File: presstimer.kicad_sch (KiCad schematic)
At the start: 28 parts, among them J1 Screw_Terminal_01x02, SW1 SW_Push, SW2 SW_Push, U1 AP7361C-33ER, U2 ESP32-S3-WROOM-1

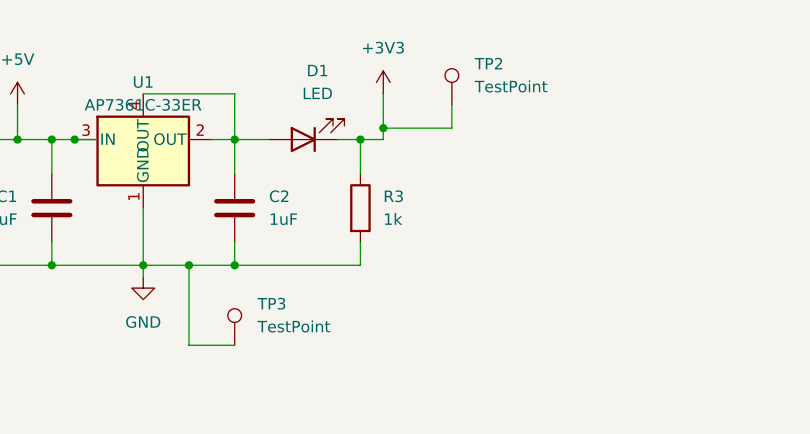
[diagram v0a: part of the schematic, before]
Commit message: fix: corrected 3v3 connections at D5, USB power to LDO, power to I2C expansion
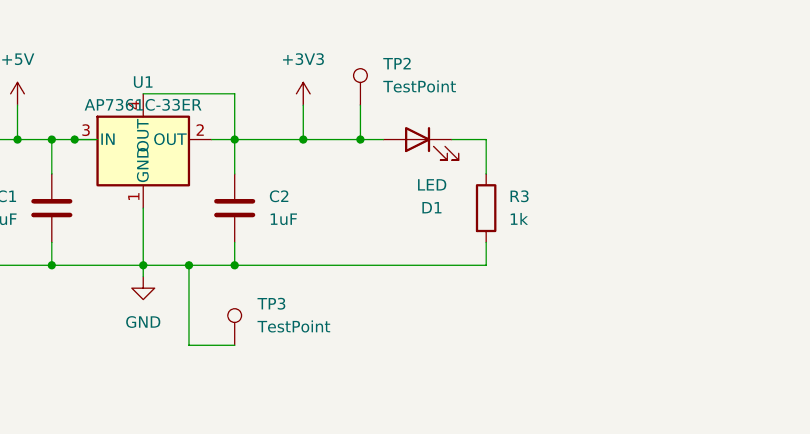
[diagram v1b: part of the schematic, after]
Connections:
- net +3V3: now also C2.1, D1.2 (A), U1.2 (OUT), U1.4 (OUT); no longer D1.1 (K), R3.1
- new net: D1.1 (K), R3.1
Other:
- moved on the sheet: D1, R3, TP2
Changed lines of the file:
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@@
 	)
 	(junction
-		(at 68.58 40.64)
+		(at 92.71 26.67)
 		(diameter 0)
 		(color 0 0 0 0)
 	)
 	(junction
-		(at 92.71 26.67)
+		(at 68.58 40.64)
 		(diameter 0)
 		(color 0 0 0 0)
 	)
 	(junction
-		(at 95.25 25.4)
+		(at 86.36 26.67)
 		(diameter 0)
 		(color 0 0 0 0)
@@
 	(wire
 		(pts
-			(xy 78.74 26.67) (xy 82.55 26.67)
+			(xy 78.74 26.67) (xy 86.36 26.67)
 		)
 		(stroke
@@
 	(wire
 		(pts
-			(xy 92.71 26.67) (xy 92.71 30.48)
+			(xy 106.68 26.67) (xy 106.68 30.48)
 		)
 		(stroke
@@
 	(wire
 		(pts
-			(xy 92.71 38.1) (xy 92.71 40.64)
+			(xy 106.68 38.1) (xy 106.68 40.64)
 		)
 		(stroke
@@
 	(wire
 		(pts
-			(xy 95.25 21.59) (xy 95.25 25.4)
+			(xy 92.71 22.86) (xy 92.71 26.67)
 		)
 		(stroke
@@
 	(wire
 		(pts
-			(xy 92.71 26.67) (xy 95.25 26.67)
-		)
-		(stroke
-			(width 0)
-			(type default)
-		)
-	)
-	(wire
-		(pts
 			(xy 182.88 60.96) (xy 182.88 59.69)
 		)
@@
 	(wire
 		(pts
-			(xy 95.25 25.4) (xy 95.25 26.67)
-		)
-		(stroke
-			(width 0)
-			(type default)
-		)
-	)
-	(wire
-		(pts
 			(xy 76.2 26.67) (xy 78.74 26.67)
 		)
@@
 	(wire
 		(pts
-			(xy 102.87 25.4) (xy 95.25 25.4)
-		)
-		(stroke
-			(width 0)
-			(type default)
-		)
-	)
-	(wire
-		(pts
 			(xy 248.92 135.89) (xy 248.92 138.43)
 		)
@@
 	(wire
 		(pts
-			(xy 102.87 22.86) (xy 102.87 25.4)
-		)
-		(stroke
-			(width 0)
-			(type default)
-		)
-	)
-	(wire
-		(pts
 			(xy 115.57 170.18) (xy 120.65 170.18)
 		)
@@
 	(wire
 		(pts
-			(xy 92.71 40.64) (xy 78.74 40.64)
+			(xy 106.68 40.64) (xy 78.74 40.64)
 		)
 		(stroke
@@
 	(wire
 		(pts
+			(xy 86.36 22.86) (xy 86.36 26.67)
+		)
+		(stroke
+			(width 0)
+			(type default)
+		)
+	)
+	(wire
+		(pts
 			(xy 72.39 146.05) (xy 78.74 146.05)
 		)
@@
 	(wire
 		(pts
-			(xy 58.42 146.05) (xy 64.77 146.05)
+			(xy 86.36 26.67) (xy 92.71 26.67)
 		)
 		(stroke
@@
 	(wire
 		(pts
-			(xy 31.75 29.21) (xy 38.1 29.21)
+			(xy 92.71 26.67) (xy 95.25 26.67)
+		)
+		(stroke
+			(width 0)
+			(type default)
+		)
+	)
+	(wire
+		(pts
+			(xy 58.42 146.05) (xy 64.77 146.05)
 		)
 		(stroke
@@
 	(wire
 		(pts
-			(xy 90.17 26.67) (xy 92.71 26.67)
+			(xy 31.75 29.21) (xy 38.1 29.21)
 		)
 		(stroke
@@
 	(wire
 		(pts
+			(xy 102.87 26.67) (xy 106.68 26.67)
+		)
+		(stroke
+			(width 0)
+			(type default)
+		)
+	)
+	(wire
+		(pts
 			(xy 58.42 26.67) (xy 60.96 26.67)
 		)
@@
 	(symbol
 		(lib_id "Connector:TestPoint")
-		(at 102.87 22.86 0)
+		(at 92.71 22.86 0)
 		(unit 1)
 		(body_style 1)
@@
 		(fields_autoplaced yes)
 		(property "Reference" "TP2"
-			(at 105.41 18.2879 0)
+			(at 95.25 18.2879 0)
 			(show_name no)
 			(do_not_autoplace no)
@@
 		)
 		(property "Value" "TestPoint"
-			(at 105.41 20.8279 0)
+			(at 95.25 20.8279 0)
 			(show_name no)
 			(do_not_autoplace no)
@@
 		)
 		(property "Footprint" "TestPoint:TestPoint_Pad_D1.5mm"
-			(at 107.95 22.86 0)
+			(at 97.79 22.86 0)
 			(hide yes)
 			(show_name no)
@@
 		)
 		(property "Datasheet" ""
-			(at 107.95 22.86 0)
+			(at 97.79 22.86 0)
 			(hide yes)
 			(show_name no)
@@
 		)
 		(property "Description" "test point"
-			(at 102.87 22.86 0)
+			(at 92.71 22.86 0)
 			(hide yes)
 			(show_name no)
@@
 	(symbol
 		(lib_id "power:+3V3")
-		(at 95.25 21.59 0)
+		(at 86.36 22.86 0)
 		(unit 1)
 		(body_style 1)
@@
 		(fields_autoplaced yes)
 		(property "Reference" "#PWR03"
-			(at 95.25 25.4 0)
+			(at 86.36 26.67 0)
 			(hide yes)
 			(show_name no)
@@
 		)
 		(property "Value" "+3V3"
-			(at 95.25 16.51 0)
+			(at 86.36 17.78 0)
 			(show_name no)
 			(do_not_autoplace no)
@@
 		)
 		(property "Footprint" ""
-			(at 95.25 21.59 0)
+			(at 86.36 22.86 0)
 			(hide yes)
 			(show_name no)
@@
 		)
 		(property "Datasheet" ""
-			(at 95.25 21.59 0)
+			(at 86.36 22.86 0)
 			(hide yes)
 			(show_name no)
@@
 		)
 		(property "Description" "Power symbol creates a global label with name \"+3V3\""
-			(at 95.25 21.59 0)
+			(at 86.36 22.86 0)
 			(hide yes)
 			(show_name no)
@@
 	(symbol
 		(lib_id "Device:R")
-		(at 92.71 34.29 0)
+		(at 106.68 34.29 0)
 		(unit 1)
 		(body_style 1)
@@
 		(fields_autoplaced yes)
 		(property "Reference" "R3"
-			(at 95.25 33.0199 0)
+			(at 109.22 33.0199 0)
 			(show_name no)
 			(do_not_autoplace no)
@@
 		)
 		(property "Value" "1k"
-			(at 95.25 35.5599 0)
+			(at 109.22 35.5599 0)
 			(show_name no)
 			(do_not_autoplace no)
@@
 		)
 		(property "Footprint" "PCM_JLCPCB:R_0603"
-			(at 90.932 34.29 90)
+			(at 104.902 34.29 90)
 			(hide yes)
 			(show_name no)
@@
 		)
 		(property "Datasheet" ""
-			(at 92.71 34.29 0)
+			(at 106.68 34.29 0)
 			(hide yes)
 			(show_name no)
@@
 		)
 		(property "Description" "Resistor"
-			(at 92.71 34.29 0)
+			(at 106.68 34.29 0)
 			(hide yes)
 			(show_name no)
@@
 		)
 		(property "LCSC" "C22548"
-			(at 95.25 33.0199 0)
+			(at 109.22 33.0199 0)
 			(hide yes)
 			(show_name no)
@@
 	(symbol
 		(lib_id "Device:LED")
-		(at 86.36 26.67 180)
+		(at 99.06 26.67 0)
+		(mirror y)
 		(unit 1)
 		(body_style 1)
@@
 		(in_pos_files yes)
 		(dnp no)
-		(fields_autoplaced yes)
 		(property "Reference" "D1"
-			(at 87.9475 19.05 0)
+			(at 100.6475 34.29 0)
 			(show_name no)
 			(do_not_autoplace no)
@@
 		)
 		(property "Value" "LED"
-			(at 87.9475 21.59 0)
+			(at 100.6475 31.75 0)
 			(show_name no)
 			(do_not_autoplace no)
@@
 		)
 		(property "Footprint" "PCM_JLCPCB:D_0805"
-			(at 86.36 26.67 0)
+			(at 99.06 26.67 0)
 			(hide yes)
 			(show_name no)
@@
 		)
 		(property "Datasheet" ""
-			(at 86.36 26.67 0)
+			(at 99.06 26.67 0)
 			(hide yes)
 			(show_name no)
@@
 		)
 		(property "Description" "Light emitting diode"
-			(at 86.36 26.67 0)
+			(at 99.06 26.67 0)
 			(hide yes)
 			(show_name no)
@@
 		)
 		(property "Sim.Pins" "1=K 2=A"
-			(at 86.36 26.67 0)
+			(at 99.06 26.67 0)
 			(hide yes)
 			(show_name no)
@@
 		)
 		(property "LCSC" "C84256"
-			(at 87.9475 19.05 0)
+			(at 100.6475 34.29 0)
 			(hide yes)
 			(show_name no)

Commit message: fixed ssr pinout
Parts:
- C3, C4, D1, D2, F1, R1, R13, R14, R2, R3: now in the parts list
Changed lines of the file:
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@@
 		(body_style 1)
 		(exclude_from_sim no)
-		(in_bom no)
+		(in_bom yes)
 		(on_board yes)
 		(in_pos_files yes)
@@
 		(body_style 1)
 		(exclude_from_sim no)
-		(in_bom no)
+		(in_bom yes)
 		(on_board yes)
 		(in_pos_files yes)
@@
 		(body_style 1)
 		(exclude_from_sim no)
-		(in_bom no)
+		(in_bom yes)
 		(on_board yes)
 		(in_pos_files yes)
@@
 		(body_style 1)
 		(exclude_from_sim no)
-		(in_bom no)
+		(in_bom yes)
 		(on_board yes)
 		(in_pos_files yes)
@@
 		(body_style 1)
 		(exclude_from_sim no)
-		(in_bom no)
+		(in_bom yes)
 		(on_board yes)
 		(in_pos_files yes)
@@
 		(body_style 1)
 		(exclude_from_sim no)
-		(in_bom no)
+		(in_bom yes)
 		(on_board yes)
 		(in_pos_files yes)
@@
 		(body_style 1)
 		(exclude_from_sim no)
-		(in_bom no)
+		(in_bom yes)
 		(on_board yes)
 		(in_pos_files yes)
@@
 		(body_style 1)
 		(exclude_from_sim no)
-		(in_bom no)
+		(in_bom yes)
 		(on_board yes)
 		(in_pos_files yes)
@@
 		(body_style 1)
 		(exclude_from_sim no)
-		(in_bom no)
+		(in_bom yes)
 		(on_board yes)
 		(in_pos_files yes)
@@
 		(body_style 1)
 		(exclude_from_sim no)
-		(in_bom no)
-		(on_board yes)
-		(in_pos_files yes)
+		(in_bom yes)
+		(on_board yes)
+		(in_pos_files yes)
